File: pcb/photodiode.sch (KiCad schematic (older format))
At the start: 10 parts, among them U3 photodiode, U4 LM324N, U5 LM324N

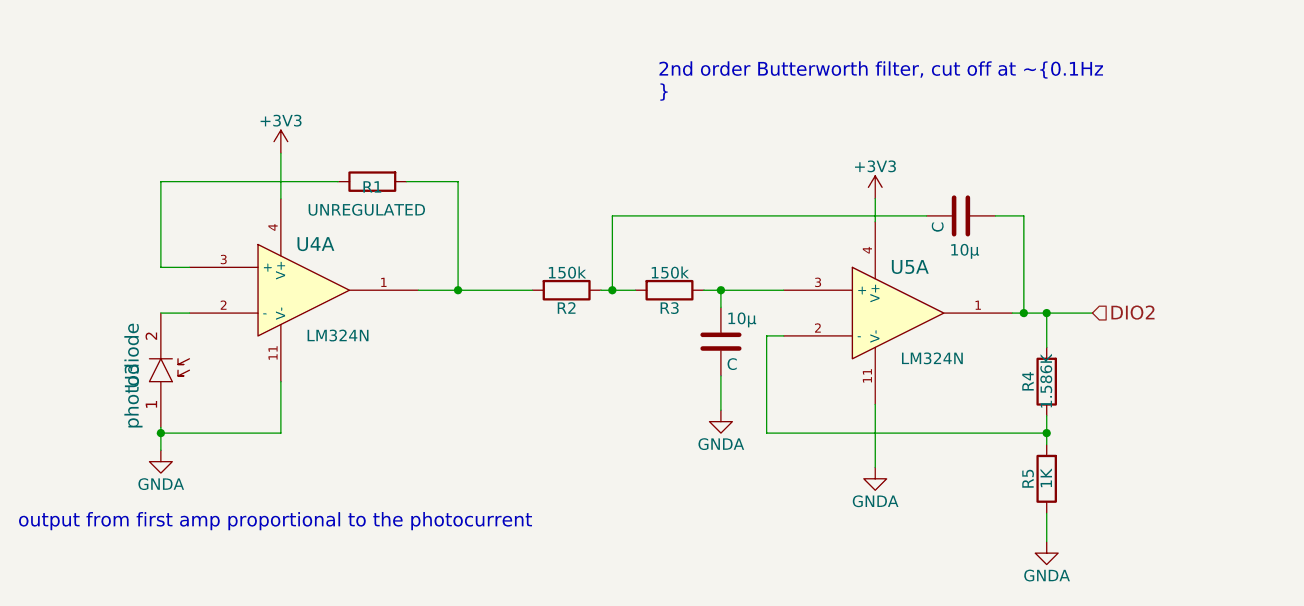
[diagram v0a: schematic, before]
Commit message: fix hierachal sheet labelling
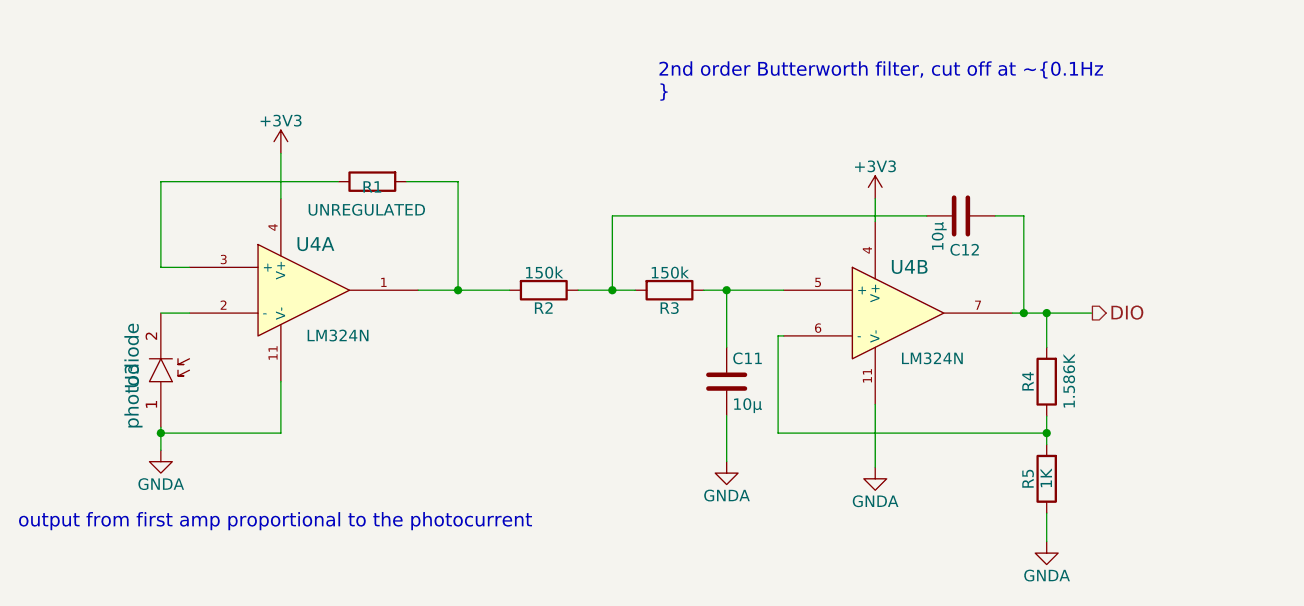
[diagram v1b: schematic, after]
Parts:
- removed U5: LM324N, symbol LM324N
- added unit 2 of U7
- C15, C16: renamed from 10µ; value C -> 10µ
- U6: renamed from U3; Order No (none) -> 1212741; Supplier (none) -> Farnell
- renumbered R1 to R11, R2 to R12, R3 to R13, R4 to R14, R5 to R15, U4 to U7
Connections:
- net +3V3: now also U7.4 (V+)
- net GNDA: now also U7.11 (V-)
- net at R14.1, R15.2: now also U7.6 (-)
- net at C15.1, R13.1: now also U7.5 (+)
- net DIO2 renamed DIO
- net DIO: now also U7.7
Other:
- moved on the sheet: C11, R2

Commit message: change filter resistor to correct value, reduce cap size (and cost)
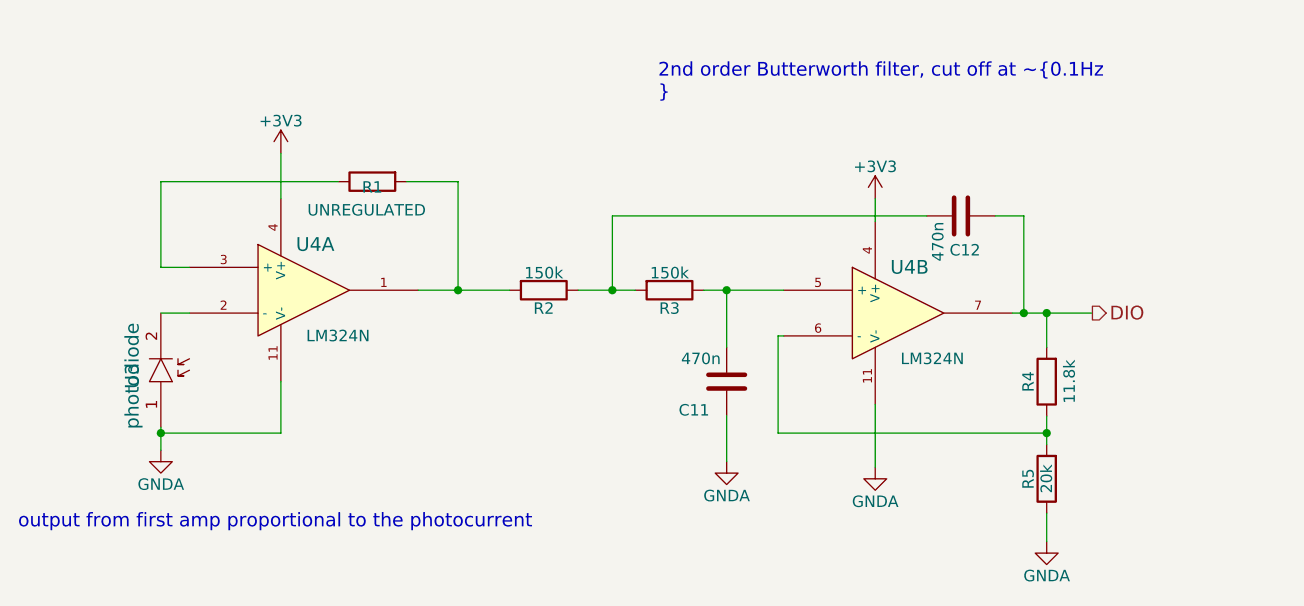
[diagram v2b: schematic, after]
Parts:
- removed C15: 10µ, symbol C
- added C11: 470n, symbol C
- C16: value 10µ -> 470n; Order No (none) -> 2429337; Supplier (none) -> Farnell
- R14: value 1.586K -> 11.8k; Order No (none) -> 2329898; Supplier (none) -> Farnell
- R15: value 1K -> 20k; Order No (none) -> 2330000; Supplier (none) -> Farnell
- U7: Order No (none) -> 1564884; Supplier (none) -> Farnell
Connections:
- net GNDA: now also C11.1
- net at R13.1, U7.5 (+): now also C11.2
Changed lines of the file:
@@
 $EndComp
 $Comp
-L GNDA #PWR21
+L GNDA #PWR021
 U 1 1 55BD9ECF
 P 3475 3925
-AR Path="/55BDA44F/55BD9ECF" Ref="#PWR21"  Part="1"
-AR Path="/55BD9D56/55BD9ECF" Ref="#PWR9"  Part="1"
-AR Path="/55BDA313/55BD9ECF" Ref="#PWR15"  Part="1"
-AR Path="/55BDA511/55BD9ECF" Ref="#PWR27"  Part="1"
-F 0 "#PWR9" H 3475 3675 50  0001 C CNN
+AR Path="/55BDA44F/55BD9ECF" Ref="#PWR021"  Part="1"
+AR Path="/55BD9D56/55BD9ECF" Ref="#PWR09"  Part="1"
+AR Path="/55BDA313/55BD9ECF" Ref="#PWR015"  Part="1"
+AR Path="/55BDA511/55BD9ECF" Ref="#PWR027"  Part="1"
+F 0 "#PWR09" H 3475 3675 50  0001 C CNN
 F 1 "GNDA" H 3475 3775 50  0000 C CNN
 F 2 "" H 3475 3925 60  0000 C CNN
@@
 F 2 "" H 4100 3225 60  0000 C CNN
 F 3 "" H 4100 3225 60  0000 C CNN
+F 4 "Farnell" H 4100 3225 60  0001 C CNN "Supplier"
+F 5 "1564884" H 4100 3225 60  0001 C CNN "Order No"
 	1    4100 3225
 	1    0    0    -1
 $EndComp
 $Comp
-L +3V3 #PWR22
+L +3V3 #PWR022
 U 1 1 55BD9EDC
 P 4000 2625
-AR Path="/55BDA44F/55BD9EDC" Ref="#PWR22"  Part="1"
-AR Path="/55BD9D56/55BD9EDC" Ref="#PWR10"  Part="1"
-AR Path="/55BDA313/55BD9EDC" Ref="#PWR16"  Part="1"
-AR Path="/55BDA511/55BD9EDC" Ref="#PWR28"  Part="1"
-F 0 "#PWR10" H 4000 2475 50  0001 C CNN
+AR Path="/55BDA44F/55BD9EDC" Ref="#PWR022"  Part="1"
+AR Path="/55BD9D56/55BD9EDC" Ref="#PWR010"  Part="1"
+AR Path="/55BDA313/55BD9EDC" Ref="#PWR016"  Part="1"
+AR Path="/55BDA511/55BD9EDC" Ref="#PWR028"  Part="1"
+F 0 "#PWR010" H 4000 2475 50  0001 C CNN
 F 1 "+3V3" H 4000 2765 50  0000 C CNN
 F 2 "" H 4000 2625 60  0000 C CNN
@@
 AR Path="/55BDA511/55BD9EFE" Ref="R19"  Part="1"
 F 0 "R4" V 7430 3625 50  0000 C CNN
-F 1 "1.586K" V 7250 3625 50  0000 C CNN
+F 1 "11.8k" V 7250 3625 50  0000 C CNN
 F 2 "" V 7280 3625 30  0000 C CNN
 F 3 "" H 7350 3625 30  0000 C CNN
+F 4 "Farnell" V 7350 3625 60  0001 C CNN "Supplier"
+F 5 "2329898" V 7350 3625 60  0001 C CNN "Order No"
 	1    7350 3625
 	-1   0    0    1
@@
 $EndComp
 $Comp
-L C C15
-U 1 1 55BD9F0E
-P 5950 3625
-AR Path="/55BDA44F/55BD9F0E" Ref="C15"  Part="1"
-AR Path="/55BD9D56/55BD9F0E" Ref="C11"  Part="1"
-AR Path="/55BDA313/55BD9F0E" Ref="C13"  Part="1"
-AR Path="/55BDA511/55BD9F0E" Ref="C17"  Part="1"
-F 0 "C11" H 5975 3725 50  0000 L CNN
-F 1 "10µ" H 5975 3525 50  0000 L CNN
-F 2 "" H 5988 3475 30  0000 C CNN
-F 3 "" H 5950 3625 60  0000 C CNN
-	1    5950 3625
-	1    0    0    -1
-$EndComp
-$Comp
-L GNDA #PWR23
+L GNDA #PWR023
 U 1 1 55BD9F18
 P 5950 3975
-AR Path="/55BDA44F/55BD9F18" Ref="#PWR23"  Part="1"
-AR Path="/55BD9D56/55BD9F18" Ref="#PWR11"  Part="1"
-AR Path="/55BDA313/55BD9F18" Ref="#PWR17"  Part="1"
-AR Path="/55BDA511/55BD9F18" Ref="#PWR29"  Part="1"
-F 0 "#PWR11" H 5950 3725 50  0001 C CNN
+AR Path="/55BDA44F/55BD9F18" Ref="#PWR023"  Part="1"
+AR Path="/55BD9D56/55BD9F18" Ref="#PWR011"  Part="1"
+AR Path="/55BDA313/55BD9F18" Ref="#PWR017"  Part="1"
+AR Path="/55BDA511/55BD9F18" Ref="#PWR029"  Part="1"
+F 0 "#PWR011" H 5950 3725 50  0001 C CNN
 F 1 "GNDA" H 5950 3825 50  0000 C CNN
 F 2 "" H 5950 3975 60  0000 C CNN
@@
 AR Path="/55BDA511/55BD9F21" Ref="R20"  Part="1"
 F 0 "R5" V 7430 4050 50  0000 C CNN
-F 1 "1K" V 7350 4050 50  0000 C CNN
+F 1 "20k" V 7350 4050 50  0000 C CNN
 F 2 "" V 7280 4050 30  0000 C CNN
 F 3 "" H 7350 4050 30  0000 C CNN
+F 4 "Farnell" V 7350 4050 60  0001 C CNN "Supplier"
+F 5 "2330000" V 7350 4050 60  0001 C CNN "Order No"
 	1    7350 4050
 	-1   0    0    1
 $EndComp
 $Comp
-L GNDA #PWR26
+L GNDA #PWR024
 U 1 1 55BD9F2A
 P 7350 4325
-AR Path="/55BDA44F/55BD9F2A" Ref="#PWR26"  Part="1"
-AR Path="/55BD9D56/55BD9F2A" Ref="#PWR14"  Part="1"
-AR Path="/55BDA313/55BD9F2A" Ref="#PWR20"  Part="1"
-AR Path="/55BDA511/55BD9F2A" Ref="#PWR32"  Part="1"
-F 0 "#PWR14" H 7350 4075 50  0001 C CNN
+AR Path="/55BDA44F/55BD9F2A" Ref="#PWR024"  Part="1"
+AR Path="/55BD9D56/55BD9F2A" Ref="#PWR012"  Part="1"
+AR Path="/55BDA313/55BD9F2A" Ref="#PWR018"  Part="1"
+AR Path="/55BDA511/55BD9F2A" Ref="#PWR030"  Part="1"
+F 0 "#PWR012" H 7350 4075 50  0001 C CNN
 F 1 "GNDA" H 7350 4175 50  0000 C CNN
 F 2 "" H 7350 4325 60  0000 C CNN
@@
 $EndComp
 $Comp
-L +3V3 #PWR24
+L +3V3 #PWR025
 U 1 1 55BD9F36
 P 6600 2825
-AR Path="/55BDA44F/55BD9F36" Ref="#PWR24"  Part="1"
-AR Path="/55BD9D56/55BD9F36" Ref="#PWR12"  Part="1"
-AR Path="/55BDA313/55BD9F36" Ref="#PWR18"  Part="1"
-AR Path="/55BDA511/55BD9F36" Ref="#PWR30"  Part="1"
-F 0 "#PWR12" H 6600 2675 50  0001 C CNN
+AR Path="/55BDA44F/55BD9F36" Ref="#PWR025"  Part="1"
+AR Path="/55BD9D56/55BD9F36" Ref="#PWR013"  Part="1"
+AR Path="/55BDA313/55BD9F36" Ref="#PWR019"  Part="1"
+AR Path="/55BDA511/55BD9F36" Ref="#PWR031"  Part="1"
+F 0 "#PWR013" H 6600 2675 50  0001 C CNN
 F 1 "+3V3" H 6600 2965 50  0000 C CNN
 F 2 "" H 6600 2825 60  0000 C CNN
@@
 DIO
 $Comp
-L GNDA #PWR25
+L GNDA #PWR026
 U 1 1 55BDC59E
 P 6600 4000
-AR Path="/55BDA44F/55BDC59E" Ref="#PWR25"  Part="1"
-AR Path="/55BD9D56/55BDC59E" Ref="#PWR13"  Part="1"
-AR Path="/55BDA313/55BDC59E" Ref="#PWR19"  Part="1"
-AR Path="/55BDA511/55BDC59E" Ref="#PWR31"  Part="1"
-F 0 "#PWR13" H 6600 3750 50  0001 C CNN
+AR Path="/55BDA44F/55BDC59E" Ref="#PWR026"  Part="1"
+AR Path="/55BD9D56/55BDC59E" Ref="#PWR014"  Part="1"
+AR Path="/55BDA313/55BDC59E" Ref="#PWR020"  Part="1"
+AR Path="/55BDA511/55BDC59E" Ref="#PWR032"  Part="1"
+F 0 "#PWR014" H 6600 3750 50  0001 C CNN
 F 1 "GNDA" H 6600 3850 50  0000 C CNN
 F 2 "" H 6600 4000 60  0000 C CNN
@@
 AR Path="/55BDA511/55BDDF51" Ref="C18"  Part="1"
 F 0 "C12" V 7125 2850 50  0000 L CNN
-F 1 "10µ" H 7000 2800 50  0000 L CNN
+F 1 "470n" H 7000 2800 50  0000 L CNN
 F 2 "" H 7013 2750 30  0000 C CNN
 F 3 "" H 6975 2900 60  0000 C CNN
+F 4 "Farnell" V 6975 2900 60  0001 C CNN "Supplier"
+F 5 "2429337" V 6975 2900 60  0001 C CNN "Order No"
 	1    6975 2900
 	0    1    1    0
@@
 	1    0    0    -1
 $EndComp
+$Comp
+L C C11
+U 1 1 55BD33E1
+P 5950 3625
+AR Path="/55BD9D56/55BD33E1" Ref="C11"  Part="1"
+AR Path="/55BDA313/55BD33E1" Ref="C13"  Part="1"
+AR Path="/55BDA44F/55BD33E1" Ref="C15"  Part="1"
+AR Path="/55BDA511/55BD33E1" Ref="C17"  Part="1"
+F 0 "C11" H 6025 3750 50  0000 L CNN
+F 1 "470n" H 5975 3525 50  0000 L CNN
+F 2 "" H 5988 3475 30  0000 C CNN
+F 3 "" H 5950 3625 60  0000 C CNN
+F 4 "Farnell" V 5950 3625 60  0001 C CNN "Supplier"
+F 5 "2429337" V 5950 3625 60  0001 C CNN "Order No"
+	1    5950 3625
+	-1   0    0    1
+$EndComp
 $EndSCHEMATC

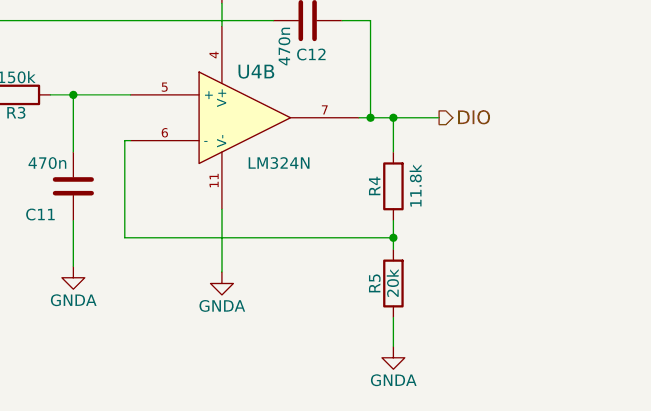
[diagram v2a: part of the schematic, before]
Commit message: add servo
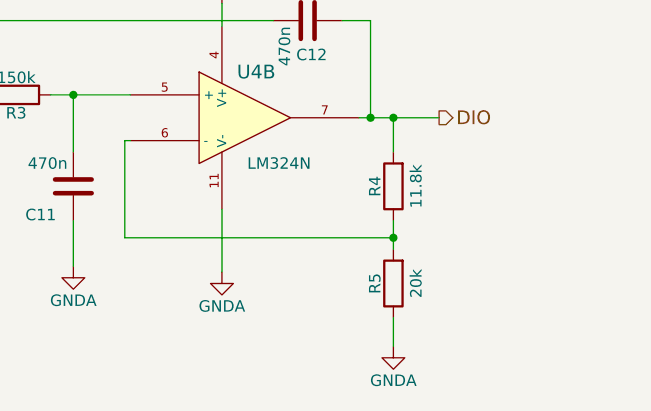
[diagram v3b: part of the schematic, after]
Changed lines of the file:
@@
 LIBS:stm32f071cbt6
 LIBS:74hc4052
+LIBS:servo
 LIBS:solarTracker-cache
 EELAYER 25 0
@@
 AR Path="/55BDA511/55BD9F21" Ref="R20"  Part="1"
 F 0 "R5" V 7430 4050 50  0000 C CNN
-F 1 "20k" V 7350 4050 50  0000 C CNN
+F 1 "20k" V 7250 4050 50  0000 C CNN
 F 2 "" V 7280 4050 30  0000 C CNN
 F 3 "" H 7350 4050 30  0000 C CNN

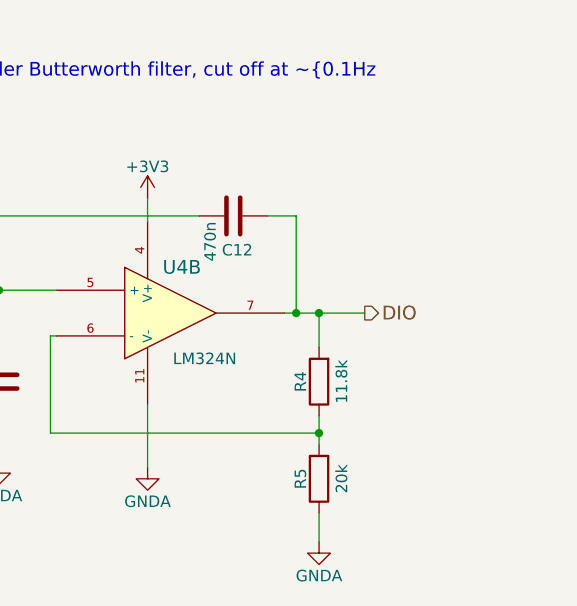
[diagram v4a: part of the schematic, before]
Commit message: add 3v3 converter
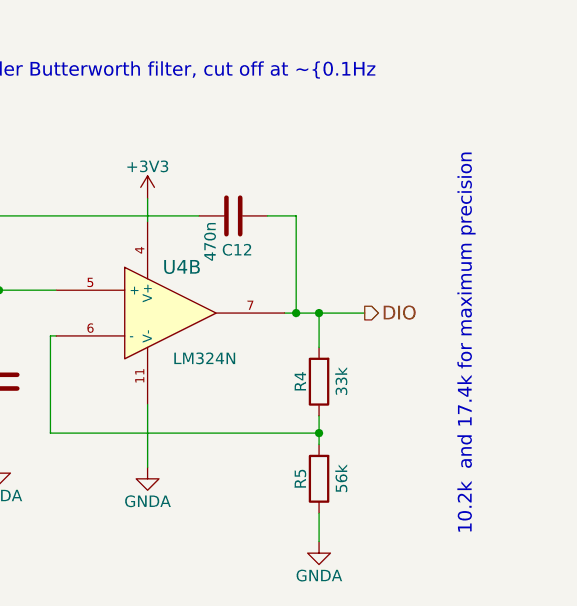
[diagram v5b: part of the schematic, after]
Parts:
- R14: value 11.8k -> 33k
- R15: value 20k -> 56k
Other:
- note added: "10.2k and 17.4k for maximum precision"
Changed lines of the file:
@@
 LIBS:servo
 LIBS:mc33063a
+LIBS:adp3335
 LIBS:solarTracker-cache
 EELAYER 25 0
@@
 AR Path="/55BDA511/55BD9EFE" Ref="R19"  Part="1"
 F 0 "R4" V 7430 3625 50  0000 C CNN
-F 1 "11.8k" V 7250 3625 50  0000 C CNN
+F 1 "33k" V 7250 3625 50  0000 C CNN
 F 2 "" V 7280 3625 30  0000 C CNN
 F 3 "" H 7350 3625 30  0000 C CNN
@@
 AR Path="/55BDA511/55BD9F21" Ref="R20"  Part="1"
 F 0 "R5" V 7430 4050 50  0000 C CNN
-F 1 "20k" V 7250 4050 50  0000 C CNN
+F 1 "56k" V 7250 4050 50  0000 C CNN
 F 2 "" V 7280 4050 30  0000 C CNN
 F 3 "" H 7350 4050 30  0000 C CNN
@@
 	-1   0    0    1
 $EndComp
+Text Notes 8025 4300 1    60   ~ 0
+10.2k  and 17.4k for maximum precision
 $EndSCHEMATC

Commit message: connect mcu to servo and mux, add level shifter
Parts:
- U7: symbol LM324N -> LM324N-RESCUE-solarTracker
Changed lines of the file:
@@
 $EndComp
 $Comp
-L LM324N U7
+L LM324N-RESCUE-solarTracker U7
 U 1 1 55BD9ED5
 P 4100 3225
@@
 AR Path="/55BDA313/55BD9ED5" Ref="U4"  Part="3"
 AR Path="/55BDA511/55BD9ED5" Ref="U7"  Part="3"
+AR Path="/55BD9ED5" Ref="U4"  Part="1"
 F 0 "U4" H 4150 3425 60  0000 C CNN
 F 1 "LM324N" H 4250 3025 50  0000 C CNN
@@
 output from first amp proportional to the photocurrent
 $Comp
-L LM324N U7
+L LM324N-RESCUE-solarTracker U7
 U 2 1 55BDFBFD
 P 6700 3325
@@
 AR Path="/55BDA313/55BDFBFD" Ref="U4"  Part="4"
 AR Path="/55BDA511/55BDFBFD" Ref="U7"  Part="4"
+AR Path="/55BDFBFD" Ref="U4"  Part="2"
 F 0 "U4" H 6750 3525 60  0000 C CNN
 F 1 "LM324N" H 6850 3125 50  0000 C CNN
